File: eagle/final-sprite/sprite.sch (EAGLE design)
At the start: 64 parts, among them J1 M20-7910442R, U1 CC430F513X, U2 LSM9DS1, U4 DRV8837, U5 ADP5092, U6 DRV8837, U7 DRV8837, X1 SPRITEPIN_SPRITE_PIN, X2 SPRITEPIN_SPRITE_PIN

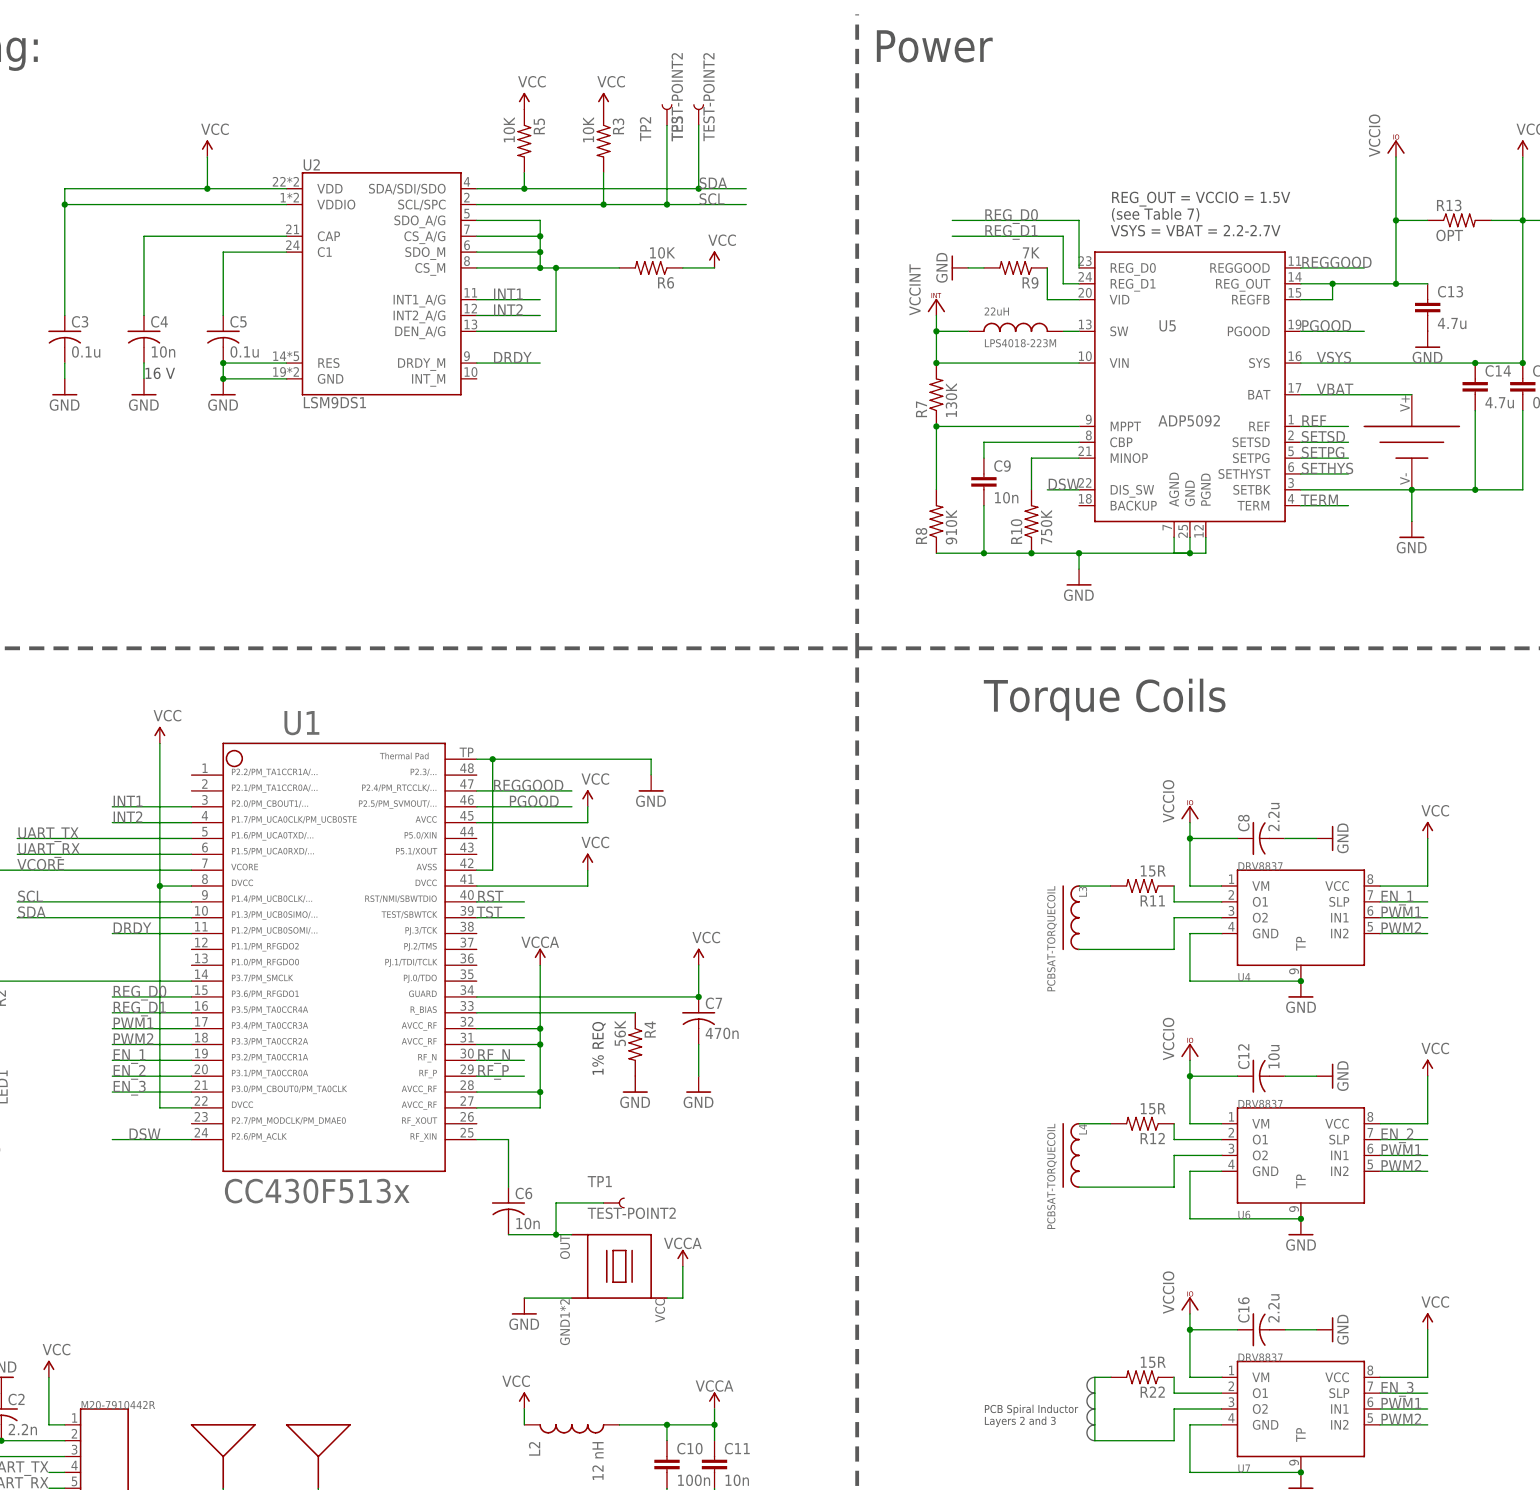
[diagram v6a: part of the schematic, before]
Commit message: Placed all components, probably
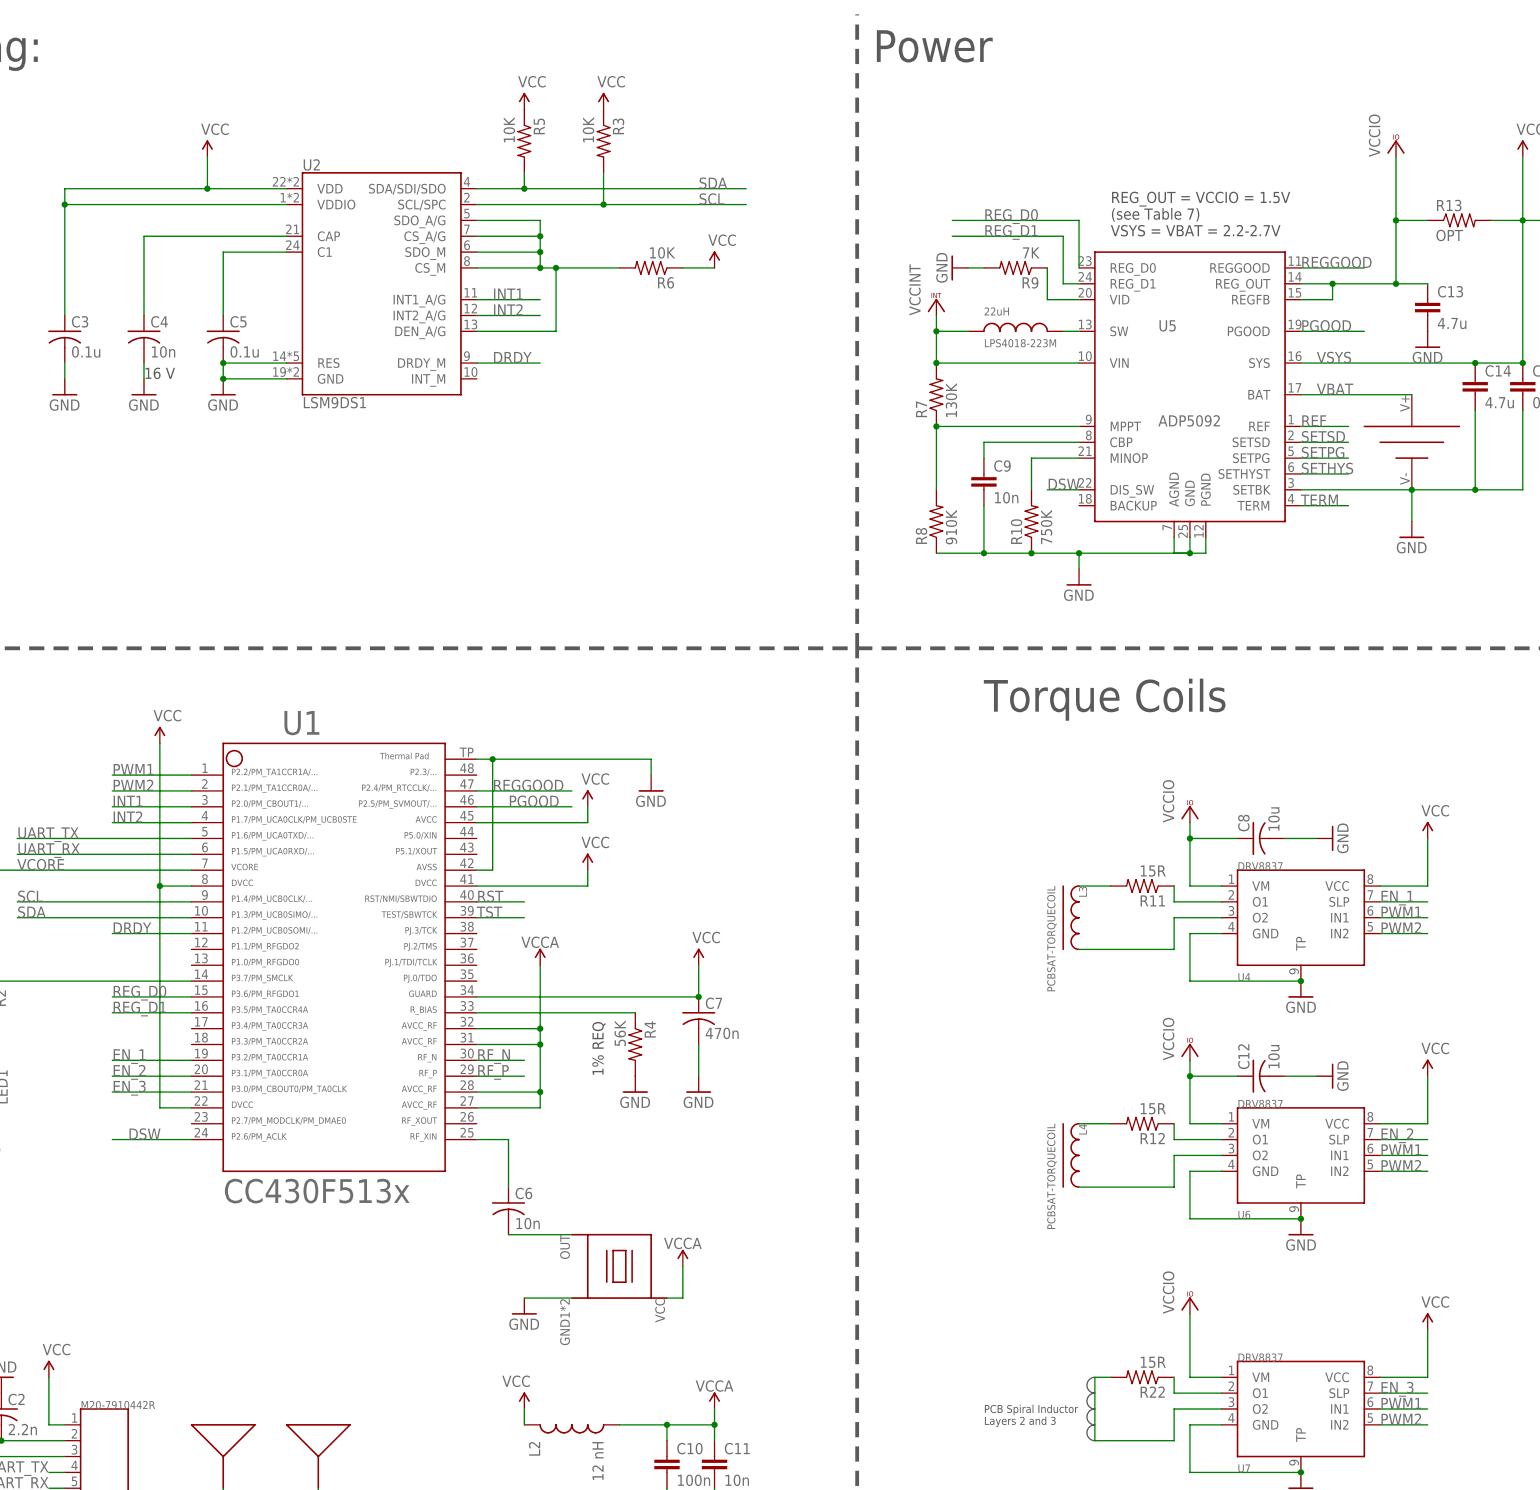
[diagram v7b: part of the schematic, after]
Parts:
- removed C16: 2.2u, rcl:C-USC0402
- removed TP1, TP2, TP3: TEST-POINT2, SparkFun-Connectors:TEST-POINT2
- C8: value 2.2u -> 10u
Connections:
- net GND: no longer C16.2
- net N$12: no longer TP1.1
- net PWM1: now also U1.1; no longer U1.17
- net PWM2: now also U1.2; no longer U1.18
- net SCL: no longer TP2.1
- net SDA: no longer TP3.1
- net VCCIO: no longer C16.1
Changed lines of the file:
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@@
 <part name="GND14" library="SparkFun" deviceset="GND" device=""/>
 <part name="GND12" library="SparkFun" deviceset="GND" device=""/>
-<part name="GND19" library="SparkFun" deviceset="GND" device=""/>
 <part name="GND25" library="SparkFun" deviceset="GND" device=""/>
 <part name="GND20" library="SparkFun" deviceset="GND" device=""/>
@@
 <part name="C7" library="rcl" library_urn="urn:adsk.eagle:library:334" deviceset="C-US" device="C0402" package3d_urn="urn:adsk.eagle:package:23626/1" value="470n"/>
 <part name="C6" library="rcl" library_urn="urn:adsk.eagle:library:334" deviceset="C-US" device="C0402" package3d_urn="urn:adsk.eagle:package:23626/1" value="10n"/>
-<part name="C8" library="rcl" library_urn="urn:adsk.eagle:library:334" deviceset="C-US" device="C0402" package3d_urn="urn:adsk.eagle:package:23626/1" value="2.2u"/>
+<part name="C8" library="rcl" library_urn="urn:adsk.eagle:library:334" deviceset="C-US" device="C0402" package3d_urn="urn:adsk.eagle:package:23626/1" value="10u"/>
 <part name="C12" library="rcl" library_urn="urn:adsk.eagle:library:334" deviceset="C-US" device="C0402" package3d_urn="urn:adsk.eagle:package:23626/1" value="10u"/>
-<part name="C16" library="rcl" library_urn="urn:adsk.eagle:library:334" deviceset="C-US" device="C0402" package3d_urn="urn:adsk.eagle:package:23626/1" value="2.2u"/>
 <part name="GND13" library="SparkFun" deviceset="GND" device=""/>
 <part name="GND22" library="SparkFun" deviceset="GND" device=""/>
@@
 <part name="P+2" library="SparkFun" deviceset="VCC" device=""/>
 <part name="GND4" library="SparkFun" deviceset="GND" device=""/>
-<part name="TP1" library="SparkFun-Connectors" library_urn="urn:adsk.eagle:library:513" deviceset="TEST-POINT" device="2" package3d_urn="urn:adsk.eagle:package:38284/1"/>
-<part name="TP2" library="SparkFun-Connectors" library_urn="urn:adsk.eagle:library:513" deviceset="TEST-POINT" device="2" package3d_urn="urn:adsk.eagle:package:38284/1"/>
-<part name="TP3" library="SparkFun-Connectors" library_urn="urn:adsk.eagle:library:513" deviceset="TEST-POINT" device="2" package3d_urn="urn:adsk.eagle:package:38284/1"/>
 <part name="A1" library="STAC" deviceset="SPRITEANTENNA_ANTENNA" device=""/>
 <part name="A2" library="STAC" deviceset="SPRITEANTENNA_ANTENNA" device=""/>
@@
 <instance part="GND14" gate="1" x="157.48" y="-223.52" rot="MR0"/>
 <instance part="GND12" gate="1" x="162.56" y="-198.12" rot="MR270"/>
-<instance part="GND19" gate="1" x="162.56" y="-276.86" rot="MR270"/>
 <instance part="GND25" gate="1" x="157.48" y="-261.62" rot="MR0"/>
 <instance part="GND20" gate="1" x="162.56" y="-236.22" rot="MR270"/>
@@
 <instance part="C8" gate="G$1" x="149.86" y="-198.12" rot="R90"/>
 <instance part="C12" gate="G$1" x="149.86" y="-236.22" rot="R90"/>
-<instance part="C16" gate="G$1" x="149.86" y="-276.86" rot="R90"/>
 <instance part="GND13" gate="1" x="101.6" y="-106.68" rot="R270"/>
 <instance part="GND22" gate="1" x="177.8" y="-119.38"/>
@@
 <instance part="P+2" gate="1" x="-43.18" y="-284.48"/>
 <instance part="GND4" gate="1" x="-43.18" y="-312.42"/>
-<instance part="TP1" gate="G$1" x="45.72" y="-256.54"/>
-<instance part="TP2" gate="G$1" x="55.88" y="-83.82" rot="R90"/>
-<instance part="TP3" gate="G$1" x="60.96" y="-83.82" rot="R90"/>
 <instance part="A1" gate="G$1" x="-15.24" y="-297.18"/>
 <instance part="A2" gate="G$1" x="0" y="-297.18"/>
@@
 </segment>
 <segment>
-<pinref part="GND19" gate="1" pin="GND"/>
-<pinref part="C16" gate="G$1" pin="2"/>
-<wire x1="160.02" y1="-276.86" x2="154.94" y2="-276.86" width="0.1524" layer="91"/>
-</segment>
-<segment>
 <pinref part="U4" gate="G$1" pin="GND"/>
 <wire x1="144.78" y1="-213.36" x2="139.7" y2="-213.36" width="0.1524" layer="91"/>
@@
 <net name="N$12" class="0">
 <segment>
-<wire x1="30.48" y1="-261.62" x2="38.1" y2="-261.62" width="0.1524" layer="91"/>
+<wire x1="30.48" y1="-261.62" x2="40.64" y2="-261.62" width="0.1524" layer="91"/>
 <pinref part="C6" gate="G$1" pin="2"/>
-<pinref part="TP1" gate="G$1" pin="1"/>
-<wire x1="38.1" y1="-261.62" x2="40.64" y2="-261.62" width="0.1524" layer="91"/>
-<wire x1="45.72" y1="-256.54" x2="38.1" y2="-256.54" width="0.1524" layer="91"/>
-<wire x1="38.1" y1="-256.54" x2="38.1" y2="-261.62" width="0.1524" layer="91"/>
-<junction x="38.1" y="-261.62"/>
 <pinref part="U3" gate="G$1" pin="OUT"/>
 </segment>
@@
 <wire x1="33.02" y1="-93.98" x2="33.02" y2="-91.44" width="0.1524" layer="91"/>
 <junction x="33.02" y="-93.98"/>
-<wire x1="33.02" y1="-93.98" x2="60.96" y2="-93.98" width="0.1524" layer="91"/>
+<wire x1="33.02" y1="-93.98" x2="68.58" y2="-93.98" width="0.1524" layer="91"/>
 <label x="60.96" y="-93.98" size="1.778" layer="95"/>
-<pinref part="TP3" gate="G$1" pin="1"/>
-<wire x1="60.96" y1="-93.98" x2="60.96" y2="-83.82" width="0.1524" layer="91"/>
-<wire x1="68.58" y1="-93.98" x2="60.96" y2="-93.98" width="0.1524" layer="91"/>
-<junction x="60.96" y="-93.98"/>
 <pinref part="R5" gate="G$1" pin="2"/>
 </segment>
@@
 <pinref part="U2" gate="G$1" pin="SCL/SPC"/>
 <wire x1="25.4" y1="-96.52" x2="45.72" y2="-96.52" width="0.1524" layer="91"/>
-<wire x1="45.72" y1="-96.52" x2="55.88" y2="-96.52" width="0.1524" layer="91"/>
-<wire x1="55.88" y1="-96.52" x2="68.58" y2="-96.52" width="0.1524" layer="91"/>
+<wire x1="45.72" y1="-96.52" x2="68.58" y2="-96.52" width="0.1524" layer="91"/>
 <wire x1="45.72" y1="-91.44" x2="45.72" y2="-96.52" width="0.1524" layer="91"/>
 <junction x="45.72" y="-96.52"/>
 <label x="60.96" y="-96.52" size="1.778" layer="95"/>
-<pinref part="TP2" gate="G$1" pin="1"/>
-<wire x1="55.88" y1="-83.82" x2="55.88" y2="-96.52" width="0.1524" layer="91"/>
-<junction x="55.88" y="-96.52"/>
 <pinref part="R3" gate="G$1" pin="2"/>
 </segment>
@@
 <junction x="172.72" y="-109.22"/>
 <pinref part="C13" gate="G$1" pin="1"/>
+<pinref part="VCC3" gate="G$1" pin="VCCIO"/>
 <pinref part="R13" gate="G$1" pin="1"/>
-<wire x1="177.8" y1="-99.06" x2="172.72" y2="-99.06" width="0.1524" layer="91"/>
+<wire x1="172.72" y1="-99.06" x2="177.8" y2="-99.06" width="0.1524" layer="91"/>
 <junction x="172.72" y="-99.06"/>
-<pinref part="VCC3" gate="G$1" pin="VCCIO"/>
 </segment>
 <segment>
@@
 <pinref part="U7" gate="G$1" pin="VM"/>
 <wire x1="144.78" y1="-284.48" x2="139.7" y2="-284.48" width="0.1524" layer="91"/>
-<wire x1="139.7" y1="-284.48" x2="139.7" y2="-276.86" width="0.1524" layer="91"/>
+<wire x1="139.7" y1="-284.48" x2="139.7" y2="-274.32" width="0.1524" layer="91"/>
 <pinref part="VCC8" gate="G$1" pin="VCCIO"/>
-<pinref part="C16" gate="G$1" pin="1"/>
-<wire x1="139.7" y1="-276.86" x2="139.7" y2="-274.32" width="0.1524" layer="91"/>
-<wire x1="147.32" y1="-276.86" x2="139.7" y2="-276.86" width="0.1524" layer="91"/>
-<junction x="139.7" y="-276.86"/>
 </segment>
 </net>
@@
 </segment>
 <segment>
-<pinref part="U1" gate="G$1" pin="18"/>
-<wire x1="-20.32" y1="-231.14" x2="-33.02" y2="-231.14" width="0.1524" layer="91"/>
-<label x="-33.02" y="-231.14" size="1.778" layer="95"/>
+<pinref part="U1" gate="G$1" pin="2"/>
+<wire x1="-20.32" y1="-190.5" x2="-33.02" y2="-190.5" width="0.1524" layer="91"/>
+<label x="-33.02" y="-190.5" size="1.778" layer="95"/>
 </segment>
 </net>
@@
 </segment>
 <segment>
-<pinref part="U1" gate="G$1" pin="17"/>
-<wire x1="-20.32" y1="-228.6" x2="-33.02" y2="-228.6" width="0.1524" layer="91"/>
-<label x="-33.02" y="-228.6" size="1.778" layer="95"/>
+<pinref part="U1" gate="G$1" pin="1"/>
+<wire x1="-20.32" y1="-187.96" x2="-33.02" y2="-187.96" width="0.1524" layer="91"/>
+<label x="-33.02" y="-187.96" size="1.778" layer="95"/>
 </segment>
 </net>
@@
 <pinref part="C15" gate="G$1" pin="1"/>
 <junction x="193.04" y="-121.92"/>
-<pinref part="R13" gate="G$1" pin="2"/>
 <wire x1="193.04" y1="-99.06" x2="193.04" y2="-88.9" width="0.1524" layer="91"/>
-<wire x1="187.96" y1="-99.06" x2="193.04" y2="-99.06" width="0.1524" layer="91"/>
 <junction x="193.04" y="-99.06"/>
 <pinref part="R14" gate="G$1" pin="1"/>
 <wire x1="193.04" y1="-99.06" x2="198.12" y2="-99.06" width="0.1524" layer="91"/>
 <label x="160.02" y="-121.92" size="1.778" layer="95"/>
-</segment>
-</net>
+<pinref part="R13" gate="G$1" pin="2"/>
+<wire x1="187.96" y1="-99.06" x2="193.04" y2="-99.06" width="0.1524" layer="91"/>
+</segment>
+</net>
